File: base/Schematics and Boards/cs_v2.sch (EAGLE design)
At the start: 55 parts, among them J1 DM3AT-SF-PEJM5, Q1 DMG3415UFY4Q-7, U1 ATSAMD51, U2 MAX77827BEWC+T, U202 COULOMB-MAX17262, U206 LOADSWITCH-MIC94162, U3 PD3S140-7, Y1 16M, Y2 ABS07-32.768KHZ-9-T

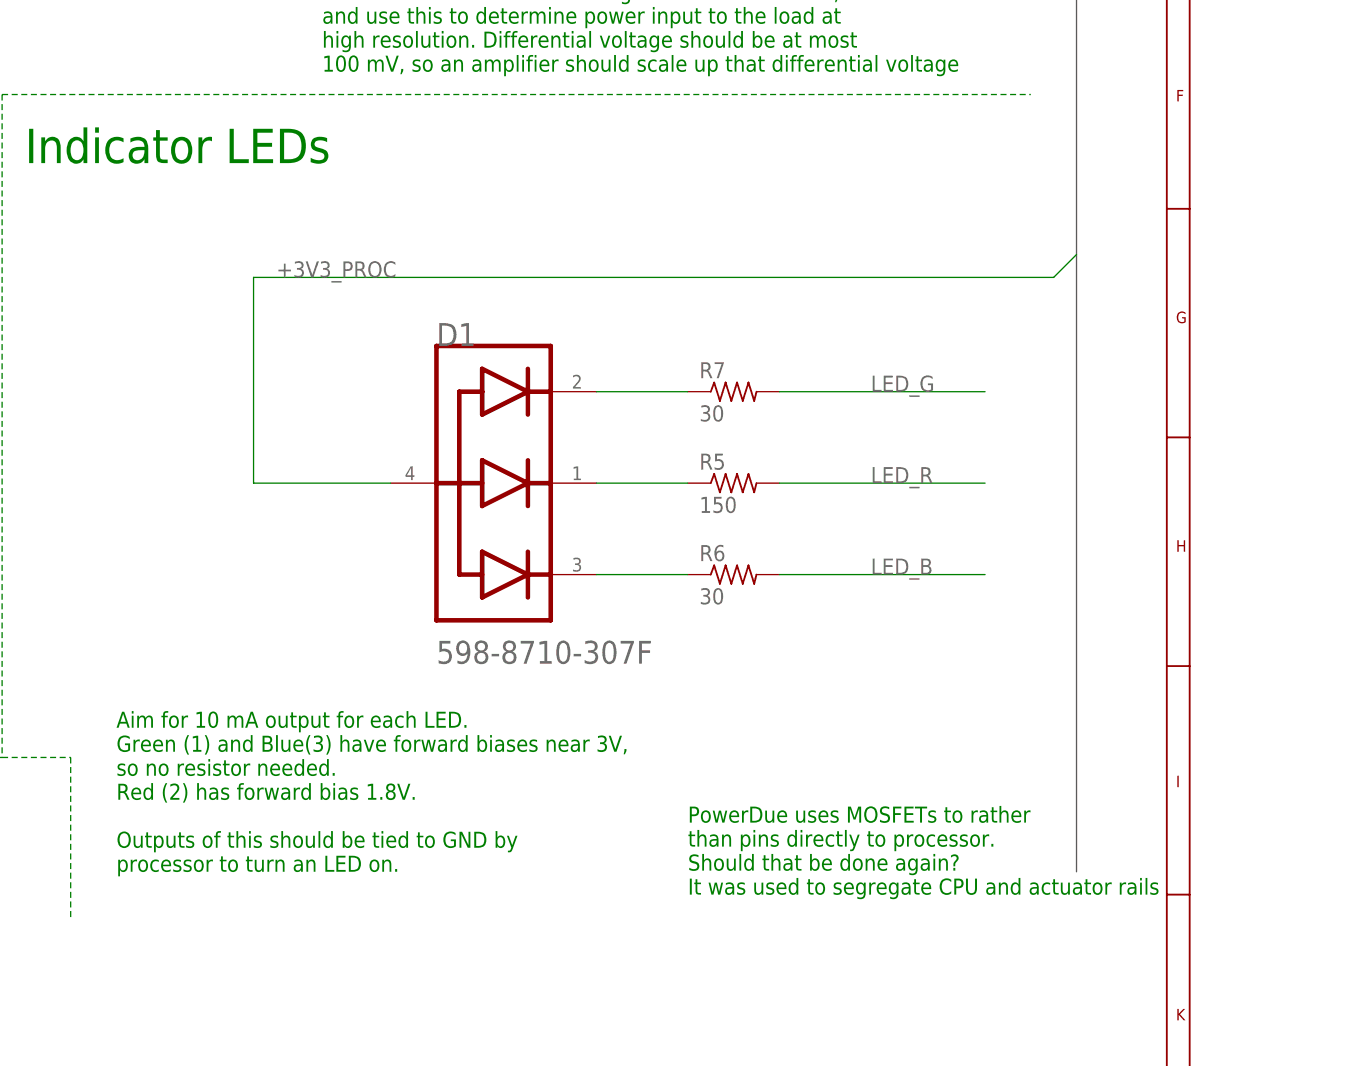
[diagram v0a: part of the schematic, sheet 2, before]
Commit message: Add NPN MOSFET to LEDs, update footprints
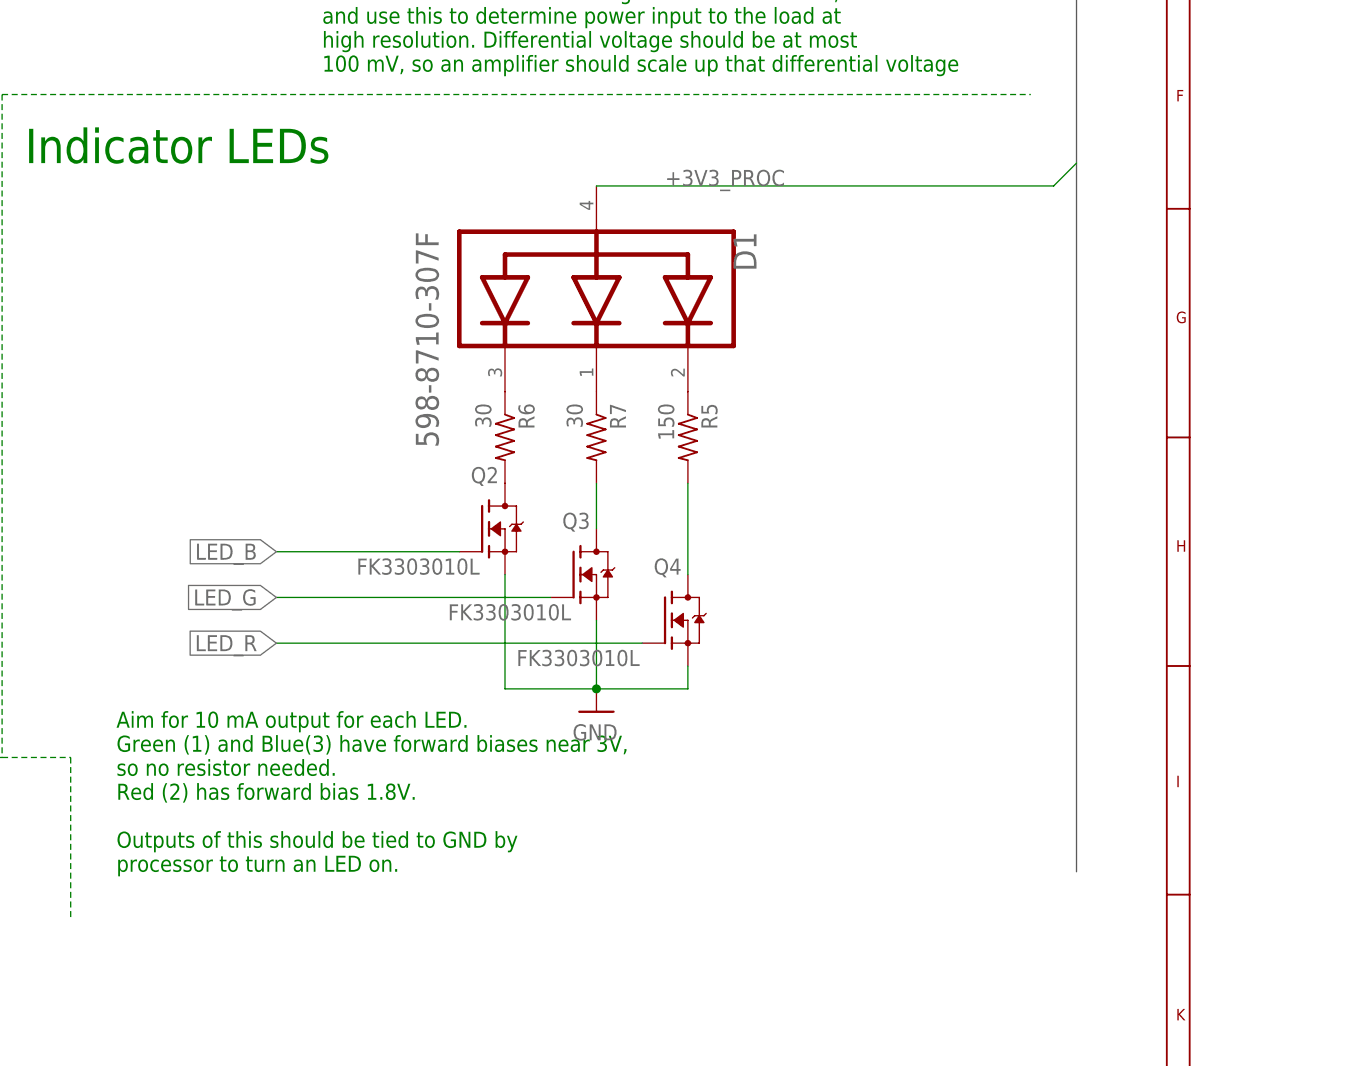
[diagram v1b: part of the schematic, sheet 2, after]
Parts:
- added Q2, Q3, Q4: FK3303010L, Switches:FK3303010L
- Q1: device Diodes:P-CH_MOSFET_DMG3415UFY4Q-7 -> Switches:DMG3415UFY4Q-7
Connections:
- new net N$15: Q2.D, R6.2
- new net N$16: Q3.D, R7.2
- new net N$17: Q4.D, R5.2
- net GND: now also Q2.S, Q3.S, Q4.S
- net LED_B: now also Q2.G; no longer R6.2
- net LED_G: now also Q3.G; no longer R7.2
- net LED_R: now also Q4.G; no longer R5.2
- net N$12: now also R7.1; no longer R5.1
- net N$14: now also R5.1; no longer R7.1
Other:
- note removed: "PowerDue uses MOSFETs to rather than pins directly to processor. Should that be done again? It was used to segregate CPU and actuator rails"
- moved on the sheet: D1, R5, R6, R7
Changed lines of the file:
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@@
 <part name="BORDER4" library="Graphics" deviceset="BORDER-CMU" device=""/>
 <part name="J_DTR" library="Connectors" deviceset="HIROSE-DF40_80-PIN_CONNECTORS" device=""/>
-<part name="Q1" library="Diodes" deviceset="P-CH_MOSFET_DMG3415UFY4Q-7" device="" value="DMG3415UFY4Q-7">
+<part name="Q1" library="Switches" deviceset="DMG3415UFY4Q-7" device="" value="DMG3415UFY4Q-7">
 <attribute name="PART_NO" value="DMG3415UFY4Q-7"/>
 </part>
@@
 <attribute name="PART_NO" value="ERJ-2RKF30R0X"/>
 </part>
+<part name="Q2" library="Switches" deviceset="FK3303010L" device=""/>
+<part name="Q3" library="Switches" deviceset="FK3303010L" device=""/>
+<part name="Q4" library="Switches" deviceset="FK3303010L" device=""/>
+<part name="GND17" library="Supplies" deviceset="GND" device=""/>
 </parts>
 <sheets>
@@
 processor to turn an LED on.</text>
 <text x="269.24" y="132.08" size="3.81" layer="91">Indicator LEDs</text>
-<text x="342.9" y="50.8" size="1.778" layer="91">PowerDue uses MOSFETs to rather
-than pins directly to processor.
-Should that be done again?
-It was used to segregate CPU and actuator rails</text>
 </plain>
 <instances>
@@
 <attribute name="VALUE" x="149.352" y="149.86" size="1.27" layer="96"/>
 </instance>
-<instance part="D1" gate="G$0" x="314.96" y="116.84" smashed="yes">
-<attribute name="NAME" x="314.96" y="114.3" size="2.54" layer="95" align="top-left"/>
-<attribute name="PART_NO" x="314.96" y="116.84" size="1.778" layer="96" display="off"/>
-</instance>
-<instance part="R5" gate="G$1" x="347.98" y="96.52" smashed="yes">
-<attribute name="NAME" x="344.17" y="98.0186" size="1.778" layer="95"/>
-<attribute name="VALUE" x="344.17" y="93.218" size="1.778" layer="96"/>
-<attribute name="PART_NO" x="347.98" y="96.52" size="1.778" layer="96" display="off"/>
-</instance>
-<instance part="R6" gate="G$1" x="347.98" y="86.36" smashed="yes">
-<attribute name="NAME" x="344.17" y="87.8586" size="1.778" layer="95"/>
-<attribute name="VALUE" x="344.17" y="83.058" size="1.778" layer="96"/>
-<attribute name="PART_NO" x="347.98" y="86.36" size="1.778" layer="96" display="off"/>
-</instance>
-<instance part="R7" gate="G$1" x="347.98" y="106.68" smashed="yes">
-<attribute name="NAME" x="344.17" y="108.1786" size="1.778" layer="95"/>
-<attribute name="VALUE" x="344.17" y="103.378" size="1.778" layer="96"/>
-<attribute name="PART_NO" x="347.98" y="106.68" size="1.778" layer="96" display="off"/>
+<instance part="D1" gate="G$0" x="353.06" y="124.46" smashed="yes" rot="R270">
+<attribute name="NAME" x="350.52" y="124.46" size="2.54" layer="95" rot="R270" align="top-left"/>
+<attribute name="PART_NO" x="353.06" y="124.46" size="1.778" layer="96" rot="R270" display="off"/>
+</instance>
+<instance part="R5" gate="G$1" x="342.9" y="101.6" smashed="yes" rot="R270">
+<attribute name="NAME" x="344.3986" y="105.41" size="1.778" layer="95" rot="R270"/>
+<attribute name="VALUE" x="339.598" y="105.41" size="1.778" layer="96" rot="R270"/>
+<attribute name="PART_NO" x="342.9" y="101.6" size="1.778" layer="96" rot="R270" display="off"/>
+</instance>
+<instance part="R6" gate="G$1" x="322.58" y="101.6" smashed="yes" rot="R270">
+<attribute name="NAME" x="324.0786" y="105.41" size="1.778" layer="95" rot="R270"/>
+<attribute name="VALUE" x="319.278" y="105.41" size="1.778" layer="96" rot="R270"/>
+<attribute name="PART_NO" x="322.58" y="101.6" size="1.778" layer="96" rot="R270" display="off"/>
+</instance>
+<instance part="R7" gate="G$1" x="332.74" y="101.6" smashed="yes" rot="R270">
+<attribute name="NAME" x="334.2386" y="105.41" size="1.778" layer="95" rot="R270"/>
+<attribute name="VALUE" x="329.438" y="105.41" size="1.778" layer="96" rot="R270"/>
+<attribute name="PART_NO" x="332.74" y="101.6" size="1.778" layer="96" rot="R270" display="off"/>
+</instance>
+<instance part="Q2" gate="A" x="320.04" y="91.44" smashed="yes">
+<attribute name="VALUE" x="306.07" y="86.36" size="1.778" layer="96"/>
+<attribute name="NAME" x="318.77" y="96.52" size="1.778" layer="95"/>
+</instance>
+<instance part="Q3" gate="A" x="330.2" y="86.36" smashed="yes">
+<attribute name="VALUE" x="316.23" y="81.28" size="1.778" layer="96"/>
+<attribute name="NAME" x="328.93" y="91.44" size="1.778" layer="95"/>
+</instance>
+<instance part="Q4" gate="A" x="340.36" y="81.28" smashed="yes">
+<attribute name="VALUE" x="323.85" y="76.2" size="1.778" layer="96"/>
+<attribute name="NAME" x="339.09" y="86.36" size="1.778" layer="95"/>
+</instance>
+<instance part="GND17" gate="1" x="332.74" y="71.12" smashed="yes">
+<attribute name="VALUE" x="330.073" y="67.945" size="1.778" layer="96"/>
 </instance>
 </instances>
@@
 <pinref part="R4" gate="G$1" pin="1"/>
 <pinref part="GND16" gate="1" pin="GND"/>
+</segment>
+<segment>
+<pinref part="Q2" gate="A" pin="S"/>
+<wire x1="322.58" y1="86.36" x2="322.58" y2="73.66" width="0.1524" layer="91"/>
+<pinref part="GND17" gate="1" pin="GND"/>
+<wire x1="322.58" y1="73.66" x2="332.74" y2="73.66" width="0.1524" layer="91"/>
+<pinref part="Q3" gate="A" pin="S"/>
+<wire x1="332.74" y1="81.28" x2="332.74" y2="73.66" width="0.1524" layer="91"/>
+<junction x="332.74" y="73.66"/>
+<pinref part="Q4" gate="A" pin="S"/>
+<wire x1="342.9" y1="76.2" x2="342.9" y2="73.66" width="0.1524" layer="91"/>
+<wire x1="342.9" y1="73.66" x2="332.74" y2="73.66" width="0.1524" layer="91"/>
 </segment>
 </net>
@@
 </segment>
 <segment>
+<label x="340.36" y="129.54" size="1.778" layer="95"/>
 <pinref part="D1" gate="G$0" pin="COMMON_ANODE"/>
-<wire x1="309.88" y1="96.52" x2="294.64" y2="96.52" width="0.1524" layer="91"/>
-<wire x1="294.64" y1="96.52" x2="294.64" y2="119.38" width="0.1524" layer="91"/>
-<wire x1="294.64" y1="119.38" x2="383.54" y2="119.38" width="0.1524" layer="91"/>
-<label x="297.18" y="119.38" size="1.778" layer="95"/>
-<wire x1="383.54" y1="119.38" x2="386.08" y2="121.92" width="0.1524" layer="91"/>
+<wire x1="332.74" y1="129.54" x2="383.54" y2="129.54" width="0.1524" layer="91"/>
+<wire x1="383.54" y1="129.54" x2="386.08" y2="132.08" width="0.1524" layer="91"/>
 </segment>
 </net>
@@
 </segment>
 </net>
-<net name="N$12" class="0">
-<segment>
-<pinref part="D1" gate="G$0" pin="GREEN_CATHODE"/>
-<pinref part="R5" gate="G$1" pin="1"/>
-<wire x1="332.74" y1="96.52" x2="342.9" y2="96.52" width="0.1524" layer="91"/>
-</segment>
-</net>
 <net name="LED_R" class="0">
 <segment>
-<pinref part="R5" gate="G$1" pin="2"/>
-<wire x1="353.06" y1="96.52" x2="375.92" y2="96.52" width="0.1524" layer="91"/>
-<label x="363.22" y="96.52" size="1.778" layer="95"/>
+<pinref part="Q4" gate="A" pin="G"/>
+<wire x1="337.82" y1="78.74" x2="297.18" y2="78.74" width="0.1524" layer="91"/>
+<label x="297.18" y="78.74" size="1.778" layer="95" rot="R180" xref="yes"/>
 </segment>
 </net>
 <net name="LED_G" class="0">
 <segment>
-<label x="363.22" y="106.68" size="1.778" layer="95"/>
-<pinref part="R7" gate="G$1" pin="2"/>
-<wire x1="353.06" y1="106.68" x2="375.92" y2="106.68" width="0.1524" layer="91"/>
-</segment>
-</net>
-<net name="LED_B" class="0">
-<segment>
-<label x="363.22" y="86.36" size="1.778" layer="95"/>
-<wire x1="353.06" y1="86.36" x2="375.92" y2="86.36" width="0.1524" layer="91"/>
-<pinref part="R6" gate="G$1" pin="2"/>
+<pinref part="Q3" gate="A" pin="G"/>
+<wire x1="327.66" y1="83.82" x2="297.18" y2="83.82" width="0.1524" layer="91"/>
+<label x="297.18" y="83.82" size="1.778" layer="95" rot="R180" xref="yes"/>
 </segment>
 </net>
@@
 <pinref part="R6" gate="G$1" pin="1"/>
 <pinref part="D1" gate="G$0" pin="BLUE_CATHODE"/>
-<wire x1="332.74" y1="86.36" x2="342.9" y2="86.36" width="0.1524" layer="91"/>
-</segment>
-</net>
-<net name="N$14" class="0">
-<segment>
-<pinref part="R7" gate="G$1" pin="1"/>
-<pinref part="D1" gate="G$0" pin="RED_CATHODE"/>
-<wire x1="332.74" y1="106.68" x2="342.9" y2="106.68" width="0.1524" layer="91"/>
 </segment>
 </net>
@@
 </segment>
 </net>
+<net name="N$15" class="0">
+<segment>
+<pinref part="R6" gate="G$1" pin="2"/>
+<pinref part="Q2" gate="A" pin="D"/>
+</segment>
+</net>
+<net name="LED_B" class="0">
+<segment>
+<pinref part="Q2" gate="A" pin="G"/>
+<wire x1="317.5" y1="88.9" x2="297.18" y2="88.9" width="0.1524" layer="91"/>
+<label x="297.18" y="88.9" size="1.778" layer="95" rot="R180" xref="yes"/>
+</segment>
+</net>
+<net name="N$12" class="0">
+<segment>
+<pinref part="D1" gate="G$0" pin="GREEN_CATHODE"/>
+<pinref part="R7" gate="G$1" pin="1"/>
+</segment>
+</net>
+<net name="N$14" class="0">
+<segment>
+<pinref part="D1" gate="G$0" pin="RED_CATHODE"/>
+<pinref part="R5" gate="G$1" pin="1"/>
+</segment>
+</net>
+<net name="N$16" class="0">
+<segment>
+<pinref part="R7" gate="G$1" pin="2"/>
+<pinref part="Q3" gate="A" pin="D"/>
+<wire x1="332.74" y1="96.52" x2="332.74" y2="91.44" width="0.1524" layer="91"/>
+</segment>
+</net>
+<net name="N$17" class="0">
+<segment>
+<pinref part="R5" gate="G$1" pin="2"/>
+<pinref part="Q4" gate="A" pin="D"/>
+<wire x1="342.9" y1="96.52" x2="342.9" y2="86.36" width="0.1524" layer="91"/>
+</segment>
+</net>

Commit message: Add a few solder jumpers and a few probe points
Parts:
- added JP1, JP2, JP3, JP4: JUMPER-SMT_2_NC_PASTE_SILK, SparkFun-Jumpers:JUMPER-SMT_2_NC_PASTE_SILK
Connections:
- new net LED_VIN: D1.COMMON_ANODE, JP1.1
- new net N$18: JP3.2, R_SENSE_DTR.2
- new net N$19: JP4.2, R_SENSE_PROC.2
- new net VDD_DBG_JMP: JP2.1, Q1.G, R4.2, U3.P
- net +3V3_DTR: now also JP3.1; no longer R_SENSE_DTR.2
- net +3V3_PROC: now also JP1.2, JP4.1; no longer D1.COMMON_ANODE, R_SENSE_PROC.2
- net VDD_DBG: now also JP2.2; no longer Q1.G, R4.2, U3.P
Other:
- moved on the sheet: C202, C206, C_REG_BIAS, C_REG_IN, C_REG_OUT, D1, J2, L3, Q1, Q2, Q3, Q4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

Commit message: Add debugger
Add 6 pin debugger, as there's no benefit to using 10 pin whatsoever. 

Also looked into digital LEDs and added a few comments in that part of schematic.
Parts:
- added J3: J-JTAG-CORTEX-NEEDLE6, Connectors:J-JTAG-CORTEX-NEEDLE6
- added R8: 1k, Resistors:R-0402
- added TP1, TP2: PTR1TP19R, TestPoints:PTR1TP19R
- J1: value DM3AT-SF-PEJM5 -> J-MICROSD-DM3AT-SF-PEJM5; device DM3AT-SF-PEJM5:DM3AT-SF-PEJM5 -> Connectors:J-MICROSD-DM3AT-SF-PEJM5
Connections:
- removed net N$6: C15.1, R1.1, R2.1, U1.NRESET
- new net DBG_SWCLK: J3.SWCLK, R8.1, U1.PA30
- new net DBG_SWDIO: J3.SWDIO, U1.PA31
- new net DTR_BUS0_AIN0: U1.PC0
- new net DTR_BUS1_AIN0: U1.PC1
- new net DTR_BUS2_AIN0: U1.PC2
- new net DTR_BUS3_AIN0: U1.PC3
- new net NRESET: C15.1, J3.NRESET, R1.1, R2.1, U1.NRESET
- net +3V3_PROC: now also J3.VTREF, R8.2
- net +3V3_SD: now also TP2.TP
- net +3V7_BATT: now also TP1.TP
- net GND: now also J3.GND
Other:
- note added: "Debugger Connect"
- note added: "WS2812 or neopixel-like?? Maybe WS2812C-2020 (2x2mm) Require 5V input, so may need LED driver. Worth??"
- note removed: "POK is open drain output. Unused, so left floating. SEL left open for 3V3 output. Both SEL and POK are center pins in WLP, so simplest to leave unused or tied to GND"
- moved on the sheet: D1, JP1, Q2, Q3, Q4, R5, R6, R7

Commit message: Wire up SERCOM 0-5 for daughter board, master 2c, & debug uart
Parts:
- added R9: 39, Resistors:R-0402
- added R_SDDAT0, R_SDDAT1, R_SDDAT2, R_SDDAT3: 100K, Resistors:R-0402
- added TP3, TP4: PTR1TP19R, TestPoints:PTR1TP19R
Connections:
- removed net ADDR_I2C_CLK: U202.SCL
- removed net ADDR_I2C_DAT: U202.SDA
- removed net SDIO_CLK: J1.CLK
- removed net SDIO_CMD: J1.CMD, R_SDCMD.1
- removed net SDIO_D0: J1.DAT0
- removed net SDIO_D1: J1.DAT1
- removed net SDIO_D2: J1.DAT2
- removed net SDIO_D3: J1.CD/DAT3
- removed net SD_DETECT: J1.A, R_SD_DET1.2
- new net DBG_SERIAL_RX: TP3.TP, U1.PB9
- new net DBG_SERIAL_TX: TP4.TP, U1.PB8
- new net DBG_SWO: J3.SWO, U1.PB30
- new net DTR_BUS0_SERCOM0_P0: U1.PC17
- new net DTR_BUS0_SERCOM0_P1: U1.PC16
- new net DTR_BUS0_SERCOM0_P2: U1.PC18
- new net DTR_BUS0_SERCOM0_P3: U1.PC19
- new net DTR_BUS1_SERCOM1_P0: U1.PA16
- new net DTR_BUS1_SERCOM1_P1: U1.PA17
- new net DTR_BUS1_SERCOM1_P2: U1.PA18
- new net DTR_BUS1_SERCOM1_P3: U1.PA19
- new net DTR_BUS2_SERCOM2_P0: U1.PB26
- new net DTR_BUS2_SERCOM2_P1: U1.PB27
- new net DTR_BUS2_SERCOM2_P2: U1.PB28
- new net DTR_BUS2_SERCOM2_P3: U1.PB29
- new net DTR_BUS3_SERCOM3_P0: U1.PA22
- new net DTR_BUS3_SERCOM3_P1: U1.PA23
- new net DTR_BUS3_SERCOM3_P2: U1.PA24
- new net DTR_BUS3_SERCOM3_P3: U1.PA25
- new net DTR_MASTER_I2C_SCL: U1.PB3, U202.SCL
- new net DTR_MASTER_I2C_SDA: U1.PB2, U202.SDA
- new net JTAG_NRESET: J3.NRESET, R9.2
- new net SD_CD: J1.A, R_SD_DET1.2, U1.PA6
- new net SD_CLK: J1.CLK, U1.PB11
- new net SD_CMD: J1.CMD, R_SDCMD.1, U1.PA8
- new net SD_D0: J1.DAT0, R_SDDAT0.1, U1.PA9
- new net SD_D1: J1.DAT1, R_SDDAT1.1, U1.PA10
- new net SD_D2: J1.DAT2, R_SDDAT2.1, U1.PA11
- new net SD_D3: J1.CD/DAT3, R_SDDAT3.1, U1.PB10
- net +3V3_SD: now also R_SDDAT0.2, R_SDDAT1.2, R_SDDAT2.2, R_SDDAT3.2
- net NRESET: now also R9.1; no longer J3.NRESET
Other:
- moved on the sheet: C16, C17, C18, C19, J1, J3, R8, R_SDCMD, R_SD_DET1, TP2, Y1, Y2
